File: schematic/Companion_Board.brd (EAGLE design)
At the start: 97 x 52 mm, 48 parts, among them Q1 16MHz

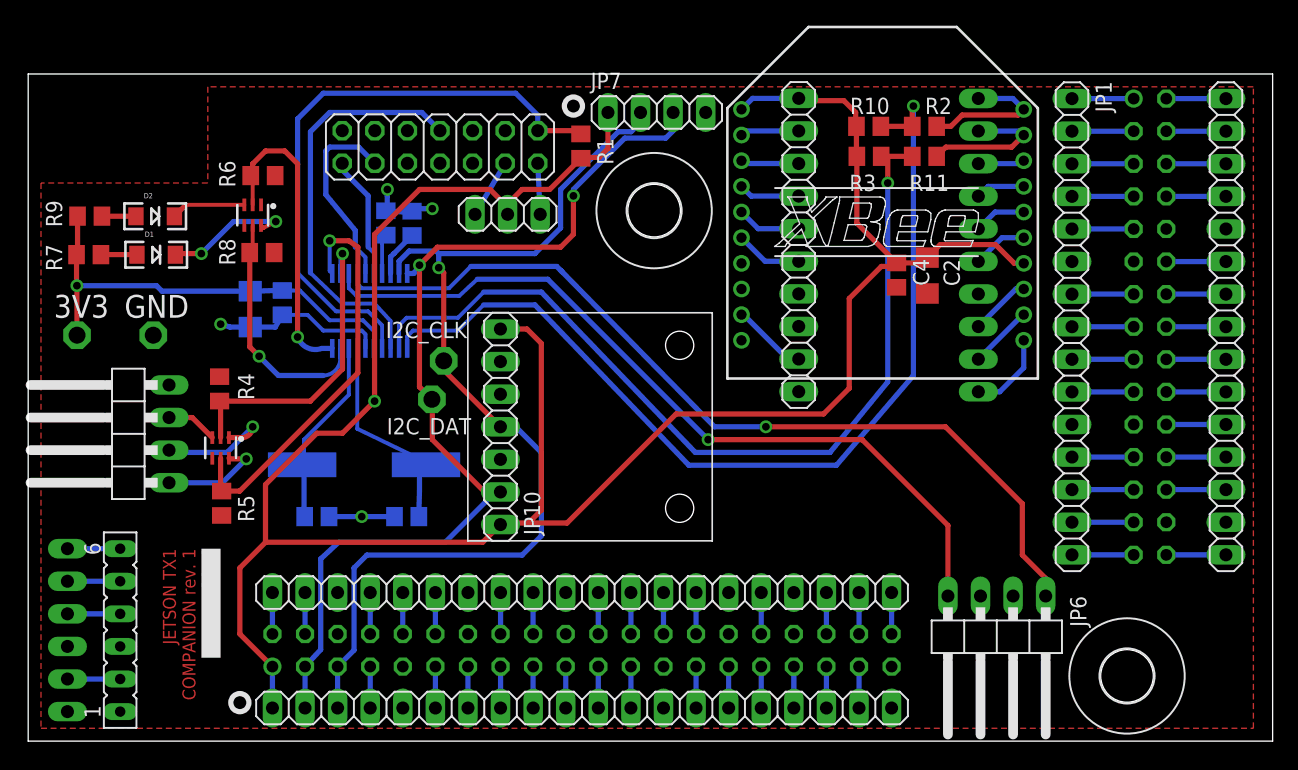
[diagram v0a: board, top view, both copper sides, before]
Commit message: Discovered a few non-connected nets.
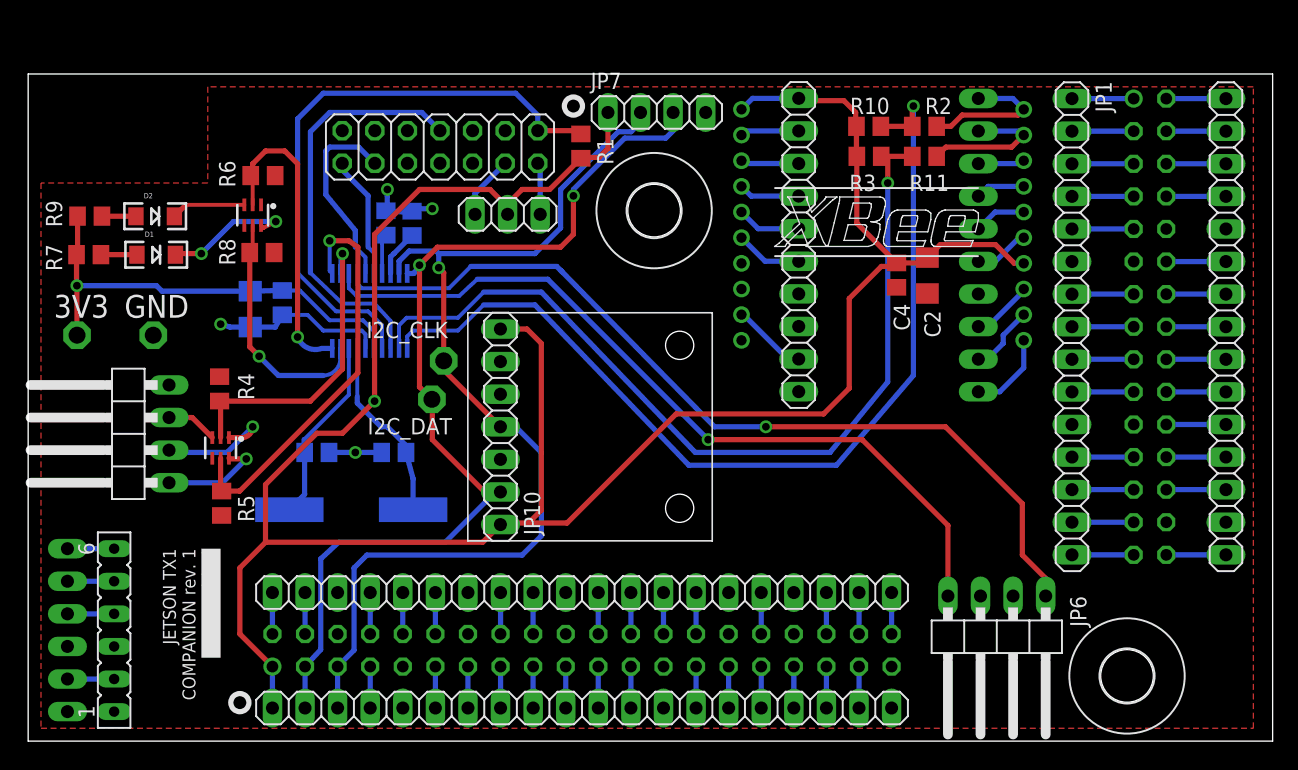
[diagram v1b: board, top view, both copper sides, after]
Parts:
- moved C5 5.10 mm to (28.5, 22.5)
- moved C6 5.00 mm to (22.5, 22.5)
- moved Q1 3.64 mm to (25.2, 18.0)
- moved J17 0.47 mm to (6.70, 8.65)
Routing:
- net N$41: track 16.9 -> 14.6 mm
- net GND: track 33.9 -> 32.9 mm

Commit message: Updated schematic with missin serial comms traces to XBee and generated finalized Gerbers.
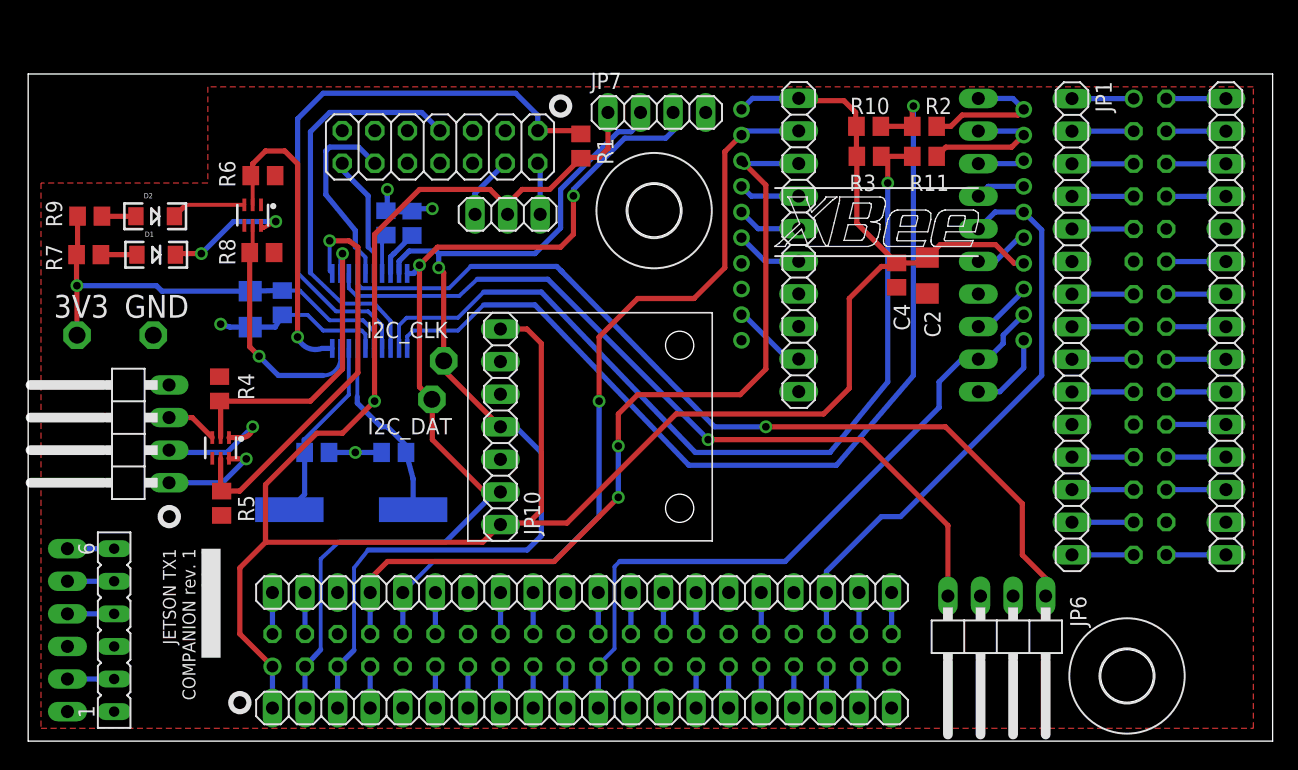
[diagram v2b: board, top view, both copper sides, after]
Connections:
- removed net N$11: JP13.3, XB1.3
- removed net N$32: JP14.6, XB1.16
- removed net N$40: JP14.2, XB1.12
- removed net N$6: JP13.2, XB1.2
- net UART1_CTS_HDR_3V3: now also JP14.6, XB1.16
- net UART1_RTS_HDR_3V3: now also JP14.2, XB1.12
- net UART1_RXD_HDR_3V3: now also JP13.2, XB1.2
- net UART1_TXD_HDR_3V3: now also JP13.3, XB1.3
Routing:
- net UART1_TXD_HDR_3V3: track 3.23 -> 67.0 mm, vias 0 -> 3
- net UART1_RXD_HDR_3V3: track 3.23 -> 62.5 mm, vias 0 -> 1
- net UART1_RTS_HDR_3V3: track 3.23 -> 53.1 mm
- net UART1_CTS_HDR_3V3: track 3.23 -> 45.4 mm
- net N$40: track 5.35 -> 0.00 mm
- net N$6: track 4.59 -> 0.00 mm
- net N$11: track 4.55 -> 0.00 mm
- net N$32: track 4.08 -> 0.00 mm

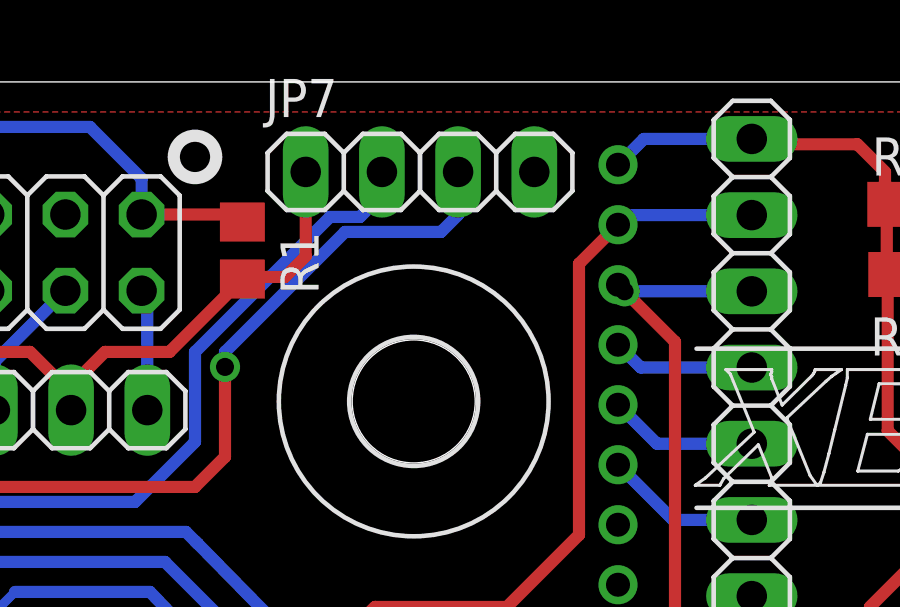
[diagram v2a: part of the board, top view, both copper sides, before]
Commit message: Updated schematic based on feedback from FreeDFM
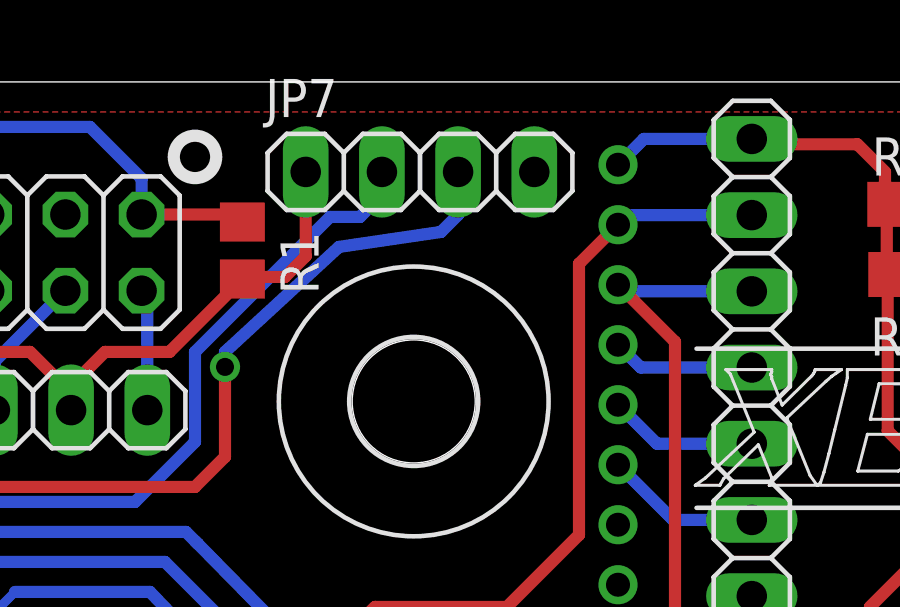
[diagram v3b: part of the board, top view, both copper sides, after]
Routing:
- net UART1_TXD_HDR_3V3: track 67.0 -> 67.3 mm, vias 3 -> 2
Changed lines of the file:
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@@
 <wire x1="50.27" y1="47.57" x2="50.27" y2="49" width="0.4064" layer="16"/>
 <wire x1="42.5" y1="42.5" x2="42.5" y2="43" width="0.4064" layer="16"/>
-<wire x1="42.5" y1="43" x2="46.5" y2="47" width="0.4064" layer="16"/>
-<wire x1="46.5" y1="47" x2="49.7" y2="47" width="0.4064" layer="16"/>
+<wire x1="42.5" y1="43" x2="46.3" y2="46.5" width="0.4064" layer="16"/>
+<wire x1="46.3" y1="46.5" x2="49.7" y2="47" width="0.4064" layer="16"/>
 <wire x1="49.7" y1="47" x2="50.27" y2="47.57" width="0.4064" layer="16"/>
 </signal>
@@
 <wire x1="28" y1="14" x2="41" y2="14" width="0.4064" layer="1"/>
 <wire x1="41" y1="14" x2="46" y2="19" width="0.4064" layer="1"/>
-<via x="55.82" y="45.02" extent="1-16" drill="0.6"/>
-<wire x1="55.82" y1="45.02" x2="57.5" y2="43.34" width="0.4064" layer="1"/>
 <wire x1="57.5" y1="43.34" x2="57.5" y2="29" width="0.4064" layer="1"/>
 <wire x1="57.5" y1="29" x2="55.5" y2="27" width="0.4064" layer="1"/>
@@
 <via x="46" y="19" extent="1-16" drill="0.6"/>
 <wire x1="46" y1="23" x2="46" y2="19" width="0.4064" layer="16"/>
+<wire x1="57.5" y1="43.34" x2="55.6" y2="45.24" width="0.4064" layer="1"/>
 </signal>
 <signal name="UART1_RXD_HDR_3V3">
